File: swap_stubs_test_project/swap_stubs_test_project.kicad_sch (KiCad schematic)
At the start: 2 parts, among them U101 74LVC541, U102 74LVC541

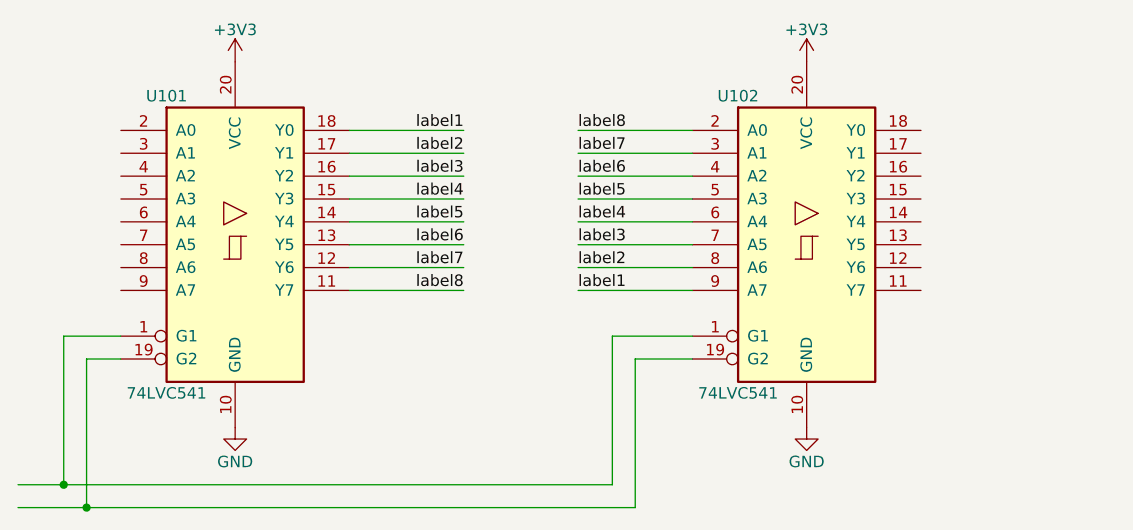
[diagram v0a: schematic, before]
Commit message: support global and hierarchical labels also
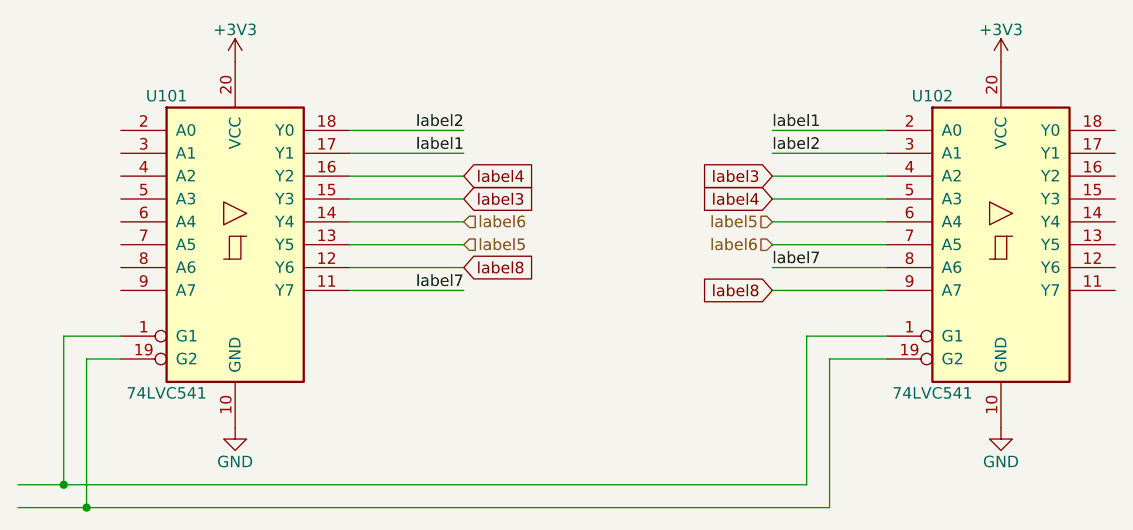
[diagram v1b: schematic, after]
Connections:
- net label1: now also U101.17 (Y1), U102.2 (A0); no longer U101.18 (Y0), U102.9 (A7)
- net label2: now also U101.18 (Y0), U102.3 (A1); no longer U101.17 (Y1), U102.8 (A6)
- net label3: now also U101.15 (Y3), U102.4 (A2); no longer U101.16 (Y2), U102.7 (A5)
- net label4: now also U101.16 (Y2), U102.5 (A3); no longer U101.15 (Y3), U102.6 (A4)
- net label5: now also U101.13 (Y5), U102.6 (A4); no longer U101.14 (Y4), U102.5 (A3)
- net label6: now also U101.14 (Y4), U102.7 (A5); no longer U101.13 (Y5), U102.4 (A2)
- net label7: now also U101.11 (Y7), U102.8 (A6); no longer U101.12 (Y6), U102.3 (A1)
- net label8: now also U101.12 (Y6), U102.9 (A7); no longer U101.11 (Y7), U102.2 (A0)
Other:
- moved on the sheet: U102
